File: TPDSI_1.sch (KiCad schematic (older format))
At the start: 2 parts, among them J1 Conn_01x02_Male, J2 Conn_01x02_Male

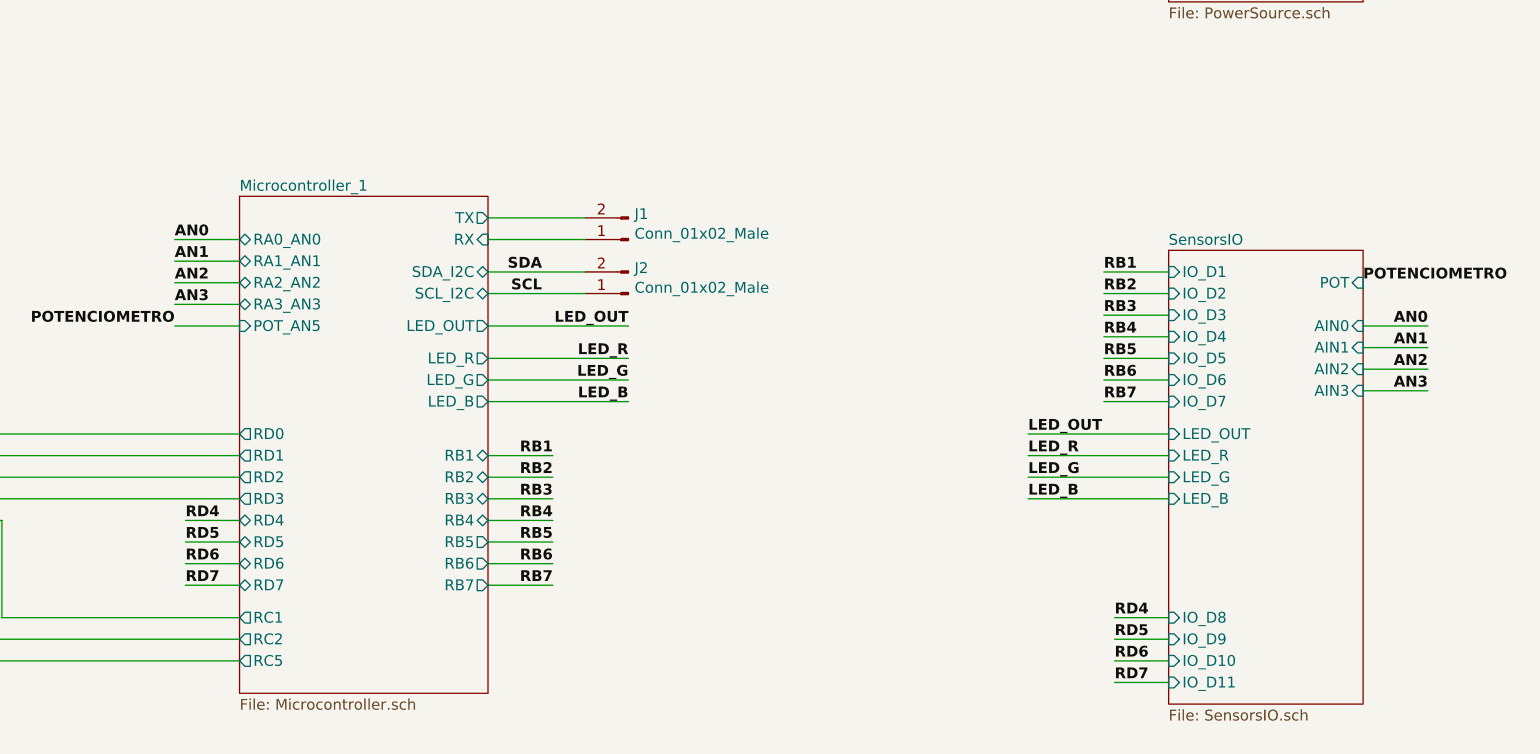
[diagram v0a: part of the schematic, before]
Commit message: Se agrega bus a jerarquia y pines de programación icsp
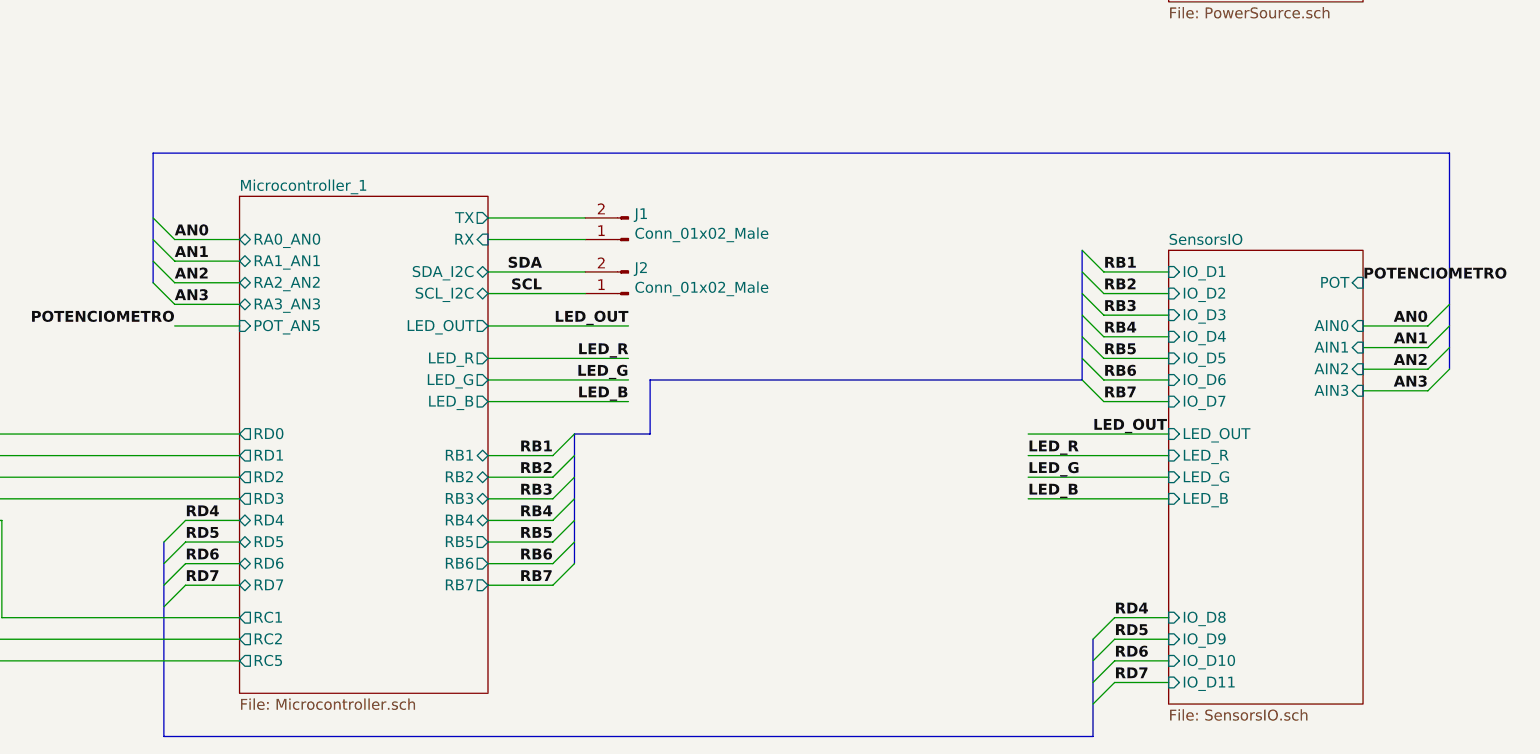
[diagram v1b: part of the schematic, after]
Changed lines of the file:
@@
 EESchema Schematic File Version 4
+LIBS:TPDSI_1-cache
 EELAYER 29 0
 EELAYER END
@@
 Sheet 1 5
 Title "Kit Development for MCU PIC"
-Date "2019-05-05"
-Rev "1.0"
+Date "2019-05-06"
+Rev "1.1"
 Comp "Julian Bustamante Narvaez"
 Comment1 ""
@@
 Wire Wire Line
 	4800 4800 5100 4800
-Text Label 5100 4200 2    50   ~ 10
-RB1
 Text Label 5100 4300 2    50   ~ 10
 RB2
@@
 POTENCIOMETRO
 Wire Wire Line
-	7950 4100 7300 4100
-Wire Wire Line
-	7950 4200 7300 4200
-Wire Wire Line
-	7950 4300 7300 4300
-Wire Wire Line
 	7950 4400 7300 4400
-Text Label 7300 4300 0    50   ~ 10
-LED_G
-Text Label 7300 4400 0    50   ~ 10
-LED_B
-Text Label 7300 4200 0    50   ~ 10
-LED_R
-Text Label 7300 4100 0    50   ~ 10
+Text Label 7600 4100 0    50   ~ 10
 LED_OUT
 Wire Wire Line
@@
 Text Label 7700 5250 0    50   ~ 10
 RD7
+Text Label 5100 4200 2    50   ~ 10
+RB1
+Entry Wire Line
+	5200 4100 5100 4200
+Entry Wire Line
+	5200 4200 5100 4300
+Entry Wire Line
+	5200 4300 5100 4400
+Entry Wire Line
+	5200 4400 5100 4500
+Entry Wire Line
+	5200 4500 5100 4600
+Entry Wire Line
+	5200 4600 5100 4700
+Entry Wire Line
+	5200 4700 5100 4800
+Entry Wire Line
+	3400 4500 3300 4600
+Entry Wire Line
+	3400 4600 3300 4700
+Entry Wire Line
+	3400 4700 3300 4800
+Entry Wire Line
+	3400 4800 3300 4900
+Entry Wire Line
+	7700 4950 7600 5050
+Entry Wire Line
+	7700 5050 7600 5150
+Entry Wire Line
+	7700 5150 7600 5250
+Entry Wire Line
+	7700 5250 7600 5350
+Wire Bus Line
+	3300 5500 7600 5500
+Entry Wire Line
+	3350 3500 3250 3400
+Entry Wire Line
+	3350 3400 3250 3300
+Entry Wire Line
+	3350 3300 3250 3200
+Entry Wire Line
+	3350 3200 3250 3100
+Entry Wire Line
+	9250 3500 9150 3600
+Entry Wire Line
+	9250 3600 9150 3700
+Entry Wire Line
+	9250 3700 9150 3800
+Entry Wire Line
+	9250 3800 9150 3900
+Wire Bus Line
+	9250 2800 3250 2800
+Entry Wire Line
+	7650 3350 7550 3250
+Entry Wire Line
+	7650 3450 7550 3350
+Entry Wire Line
+	7650 3550 7550 3450
+Entry Wire Line
+	7650 3650 7550 3550
+Entry Wire Line
+	7650 3750 7550 3650
+Entry Wire Line
+	7650 3850 7550 3750
+Entry Wire Line
+	7650 3950 7550 3850
+Text Label 7300 4200 0    50   ~ 10
+LED_R
+Text Label 7300 4400 0    50   ~ 10
+LED_B
+Text Label 7300 4300 0    50   ~ 10
+LED_G
+Wire Wire Line
+	7950 4300 7300 4300
+Wire Wire Line
+	7950 4200 7300 4200
+Wire Wire Line
+	7950 4100 7300 4100
+Wire Bus Line
+	7550 3850 5550 3850
+Wire Bus Line
+	5550 3850 5550 4100
+Wire Bus Line
+	5200 4100 5550 4100
+Wire Bus Line
+	9250 2800 9250 3800
+Wire Bus Line
+	3250 2800 3250 3400
+Wire Bus Line
+	7600 5050 7600 5500
+Wire Bus Line
+	3300 4600 3300 5500
+Wire Bus Line
+	5200 4100 5200 4700
+Wire Bus Line
+	7550 3250 7550 3850
 $EndSCHEMATC

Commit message: Se Organiza conexiones de alimentacion con elementos de la biblioteca power, se quitan algunas etiquetas y se coloca la fuente en hoja principal
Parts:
- added C1: 0.1uF, symbol Device:CP
- added C2: 22uF, symbol Device:CP
- added C3: 1uF, symbol Device:CP
- added C4: 10uF, symbol Device:CP
- added D1: D, symbol Device:D
- added D2: LED, symbol Device:LED
- added D3: D_TVS_DESD5V0S1BA-7DITR-ND, symbol Device:D_TVS
- added D6: D_TVS_3V3, symbol Device:D_TVS
- added J7: Conn_01x02_Male, symbol Connector:Conn_01x02_Male
- added R12: 330, symbol Device:R
- added U3: MC7805_TO252-3(DPACK), symbol J_ReguladorLinear:MC7805_TO252-3(DPACK)
- added U4: TLV2217_TO252-3, symbol J_ReguladorLinear:TLV2217_TO252-3
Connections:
- net labels added: +3.3V, +5V, 9V0, GND
- net labels removed: +3V3, +5V0
- wire segments 58 -> 90
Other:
- note added: "Power Source 5VDC and 3.3VDC"
- moved on the sheet: J1, J2

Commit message: Se agregan recomendaciones izq->dcha (In/Out), se Reorganiza jerarquía y bus de datos, se coloca graphics lines para indicar submodulos
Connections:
- wire segments 90 -> 80

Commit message: Se agrega ubicación de componentes, asociación de footprint, pendiente Ruteo.
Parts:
- C1: value 0.1uF -> 1uF; footprint (none) -> Capacitor_Tantalum_SMD:CP_EIA-3528-21_Kemet-B; Part Number (none) -> 399-14253-2-ND
- C2: footprint (none) -> Capacitor_Tantalum_SMD:CP_EIA-7343-20_Kemet-V; Part Number (none) -> P16517DKR-ND
- C3: footprint (none) -> Capacitor_Tantalum_SMD:CP_EIA-3528-21_Kemet-B
- C4: footprint (none) -> Capacitor_Tantalum_SMD:CP_EIA-7343-20_Kemet-V; Part number (none) -> 399-16038-1-ND
- D1: footprint (none) -> Diode_SMD:D_SOD-123; PArt Number (none) -> 1N4148W-FDICT-ND
- D2: footprint (none) -> LED_SMD:LED_0603_1608Metric_Castellated; PArt Number (none) -> 160-1446-6-ND
- D3: footprint (none) -> Diode_SMD:D_SOD-123
- D6: footprint (none) -> Diode_SMD:D_SOD-123; Part Number (none) -> 641-1985-1-ND
- J1, J2, J7: footprint (none) -> Connector_PinSocket_2.54mm:PinSocket_1x02_P2.54mm_Vertical
- R12: footprint (none) -> Resistor_SMD:R_0603_1608Metric_Pad1.05x0.95mm_HandSolder
- U3, U4: footprint (none) -> Package_TO_SOT_SMD:TO-252-2
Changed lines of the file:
@@
 AR Path="/5CDBB83D" Ref="C1"  Part="1"
 F 0 "C1" H 2168 1596 50  0000 L CNN
-F 1 "0.1uF" H 2168 1505 50  0000 L CNN
-F 2 "" H 2088 1400 50  0001 C CNN
+F 1 "1uF" H 2168 1505 50  0000 L CNN
+F 2 "Capacitor_Tantalum_SMD:CP_EIA-3528-21_Kemet-B" H 2088 1400 50  0001 C CNN
 F 3 "~" H 2050 1550 50  0001 C CNN
+F 4 "	399-14253-2-ND" H 2050 1550 50  0001 C CNN "Part Number"
 	1    2050 1550
 	1    0    0    -1
@@
 F 0 "C2" H 3018 1596 50  0000 L CNN
 F 1 "22uF" H 3018 1505 50  0000 L CNN
-F 2 "" H 2938 1400 50  0001 C CNN
+F 2 "Capacitor_Tantalum_SMD:CP_EIA-7343-20_Kemet-V" H 2938 1400 50  0001 C CNN
 F 3 "~" H 2900 1550 50  0001 C CNN
+F 4 "P16517DKR-ND" H 2900 1550 50  0001 C CNN "Part Number"
 	1    2900 1550
 	1    0    0    -1
@@
 F 0 "U4" H 4200 1215 50  0000 C CNN
 F 1 "TLV2217_TO252-3" H 4200 1124 50  0000 C CNN
-F 2 "" H 4000 1050 50  0001 C CNN
+F 2 "Package_TO_SOT_SMD:TO-252-2" H 4000 1050 50  0001 C CNN
 F 3 "http://www.ti.com/lit/ds/symlink/tlv2217.pdf" H 4000 1050 50  0001 C CNN
 F 4 "296-19786-1-ND" H 4000 1100 50  0001 C CNN " Part Number"
@@
 AR Path="/5CCF7078/5CDBB851" Ref="U?"  Part="1"
 AR Path="/5CDBB851" Ref="U3"  Part="1"
+AR Path="/5CCF70C1/5CDBB851" Ref="U3"  Part="1"
 F 0 "U3" H 2450 1215 50  0000 C CNN
 F 1 "MC7805_TO252-3(DPACK)" H 2450 1124 50  0000 C CNN
-F 2 "" H 2250 1050 50  0001 C CNN
+F 2 "Package_TO_SOT_SMD:TO-252-2" H 2250 1050 50  0001 C CNN
 F 3 "https://www.onsemi.com/pub/Collateral/MC7800-D.PDF" H 2250 1050 50  0001 C CNN
 F 4 "MC7805BDTRKGOSCT-ND" H 2450 1300 50  0001 C CNN " Part Number"
@@
 F 0 "C3" H 3818 1596 50  0000 L CNN
 F 1 "1uF" H 3818 1505 50  0000 L CNN
-F 2 "" H 3738 1400 50  0001 C CNN
+F 2 "Capacitor_Tantalum_SMD:CP_EIA-3528-21_Kemet-B" H 3738 1400 50  0001 C CNN
 F 3 "~" H 3700 1550 50  0001 C CNN
 	1    3700 1550
@@
 F 0 "C4" H 4768 1596 50  0000 L CNN
 F 1 "10uF" H 4768 1505 50  0000 L CNN
-F 2 "" H 4688 1400 50  0001 C CNN
+F 2 "Capacitor_Tantalum_SMD:CP_EIA-7343-20_Kemet-V" H 4688 1400 50  0001 C CNN
 F 3 "~" H 4650 1550 50  0001 C CNN
+F 4 "399-16038-1-ND" H 4650 1550 50  0001 C CNN "Part number"
 	1    4650 1550
 	1    0    0    -1
@@
 F 0 "D1" H 1550 1366 50  0000 C CNN
 F 1 "D" H 1550 1275 50  0000 C CNN
-F 2 "" H 1550 1150 50  0001 C CNN
+F 2 "Diode_SMD:D_SOD-123" H 1550 1150 50  0001 C CNN
 F 3 "~" H 1550 1150 50  0001 C CNN
+F 4 "1N4148W-FDICT-ND" H 1550 1150 50  0001 C CNN "PArt Number"
 	1    1550 1150
 	-1   0    0    -1
@@
 F 0 "D6" V 5104 1629 50  0000 L CNN
 F 1 "D_TVS_3V3" H 5000 1850 50  0000 L CNN
-F 2 "" H 5150 1550 50  0001 C CNN
+F 2 "Diode_SMD:D_SOD-123" H 5150 1550 50  0001 C CNN
 F 3 "~" H 5150 1550 50  0001 C CNN
+F 4 "641-1985-1-ND" V 5150 1550 50  0001 C CNN "Part Number"
 	1    5150 1550
 	0    1    1    0
@@
 F 0 "D2" V 1789 1583 50  0000 R CNN
 F 1 "LED" V 1698 1583 50  0000 R CNN
-F 2 "" H 1750 1700 50  0001 C CNN
+F 2 "LED_SMD:LED_0603_1608Metric_Castellated" H 1750 1700 50  0001 C CNN
 F 3 "~" H 1750 1700 50  0001 C CNN
+F 4 "	160-1446-6-ND" V 1750 1700 50  0001 C CNN "PArt Number"
 	1    1750 1700
 	0    -1   -1   0
@@
 F 0 "R12" H 1820 1346 50  0000 L CNN
 F 1 "330" H 1820 1255 50  0000 L CNN
-F 2 "" V 1680 1300 50  0001 C CNN
+F 2 "Resistor_SMD:R_0603_1608Metric_Pad1.05x0.95mm_HandSolder" V 1680 1300 50  0001 C CNN
 F 3 "~" H 1750 1300 50  0001 C CNN
 	1    1750 1300
@@
 F 0 "D3" V 3154 1629 50  0000 L CNN
 F 1 "D_TVS_DESD5V0S1BA-7DITR-ND" V 3800 750 50  0001 L CNN
-F 2 "" H 3200 1550 50  0001 C CNN
+F 2 "Diode_SMD:D_SOD-123" H 3200 1550 50  0001 C CNN
 F 3 "~" H 3200 1550 50  0001 C CNN
 	1    3200 1550
@@
 F 0 "J7" H 1150 1350 50  0000 C CNN
 F 1 "Conn_01x02_Male" H 1000 950 50  0000 C CNN
-F 2 "" H 1050 1150 50  0001 C CNN
+F 2 "Connector_PinSocket_2.54mm:PinSocket_1x02_P2.54mm_Vertical" H 1050 1150 50  0001 C CNN
 F 3 "~" H 1050 1150 50  0001 C CNN
 	1    1050 1150
@@
 F 0 "J1" H 7322 3732 50  0000 R CNN
 F 1 "Conn_01x02_Male" H 7322 3823 50  0000 R CNN
-F 2 "" H 7350 3850 50  0001 C CNN
+F 2 "Connector_PinSocket_2.54mm:PinSocket_1x02_P2.54mm_Vertical" H 7350 3850 50  0001 C CNN
 F 3 "~" H 7350 3850 50  0001 C CNN
 	1    7350 3850
@@
 F 0 "J2" H 7322 3982 50  0000 R CNN
 F 1 "Conn_01x02_Male" H 7322 4073 50  0000 R CNN
-F 2 "" H 7350 4100 50  0001 C CNN
+F 2 "Connector_PinSocket_2.54mm:PinSocket_1x02_P2.54mm_Vertical" H 7350 4100 50  0001 C CNN
 F 3 "~" H 7350 4100 50  0001 C CNN
 	1    7350 4100

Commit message: Se reorganiza componenentes lineas mas limpias y analógicas mas cerca,Se cambia potenciometro y bornera de alimentación, se colocan perforaciones en la tarjeta
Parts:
- removed J7: Conn_01x02_Male, Connector_PinSocket_2.54mm:PinSocket_1x02_P2.54mm_Vertical, symbol Connector:Conn_01x02_Male
- added H1, H2, H3, H4: MountingHole, MountingHole:MountingHole_3.2mm_M3, symbol Mechanical:MountingHole
- added J7: Screw_Terminal_01x02, TerminalBlock:TerminalBlock_bornier-2_P5.08mm, symbol Connector:Screw_Terminal_01x02
- U3: symbol J_ReguladorLinear:MC7805_TO252-3(DPACK) -> TPDSI_1-rescue:MC7805_TO252-3(DPACK)-J_ReguladorLinear
- U4: symbol J_ReguladorLinear:TLV2217_TO252-3 -> TPDSI_1-rescue:TLV2217_TO252-3-J_ReguladorLinear
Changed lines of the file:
@@
 $EndComp
 $Comp
-L J_ReguladorLinear:TLV2217_TO252-3 U?
+L TPDSI_1-rescue:TLV2217_TO252-3-J_ReguladorLinear U?
 U 1 1 5CDBB84A
 P 4000 1050
@@
 $EndComp
 $Comp
-L J_ReguladorLinear:MC7805_TO252-3(DPACK) U?
+L TPDSI_1-rescue:MC7805_TO252-3(DPACK)-J_ReguladorLinear U?
 U 1 1 5CDBB851
 P 2250 1050
@@
 Wire Wire Line
 	1350 1250 1350 1800
-$Comp
-L Connector:Conn_01x02_Male J7
-U 1 1 5CF0DD35
-P 1050 1150
-F 0 "J7" H 1150 1350 50  0000 C CNN
-F 1 "Conn_01x02_Male" H 1000 950 50  0000 C CNN
-F 2 "Connector_PinSocket_2.54mm:PinSocket_1x02_P2.54mm_Vertical" H 1050 1150 50  0001 C CNN
-F 3 "~" H 1050 1150 50  0001 C CNN
-	1    1050 1150
-	1    0    0    -1
-$EndComp
 Text Label 1300 1150 0    50   ~ 0
 9V0
@@
 Wire Wire Line
 	3650 5850 5550 5850
+$Comp
+L Connector:Screw_Terminal_01x02 J7
+U 1 1 5CF6B993
+P 1050 1250
+F 0 "J7" H 968 925 50  0000 C CNN
+F 1 "Screw_Terminal_01x02" H 968 1016 50  0000 C CNN
+F 2 "TerminalBlock:TerminalBlock_bornier-2_P5.08mm" H 1050 1250 50  0001 C CNN
+F 3 "~" H 1050 1250 50  0001 C CNN
+	1    1050 1250
+	-1   0    0    1
+$EndComp
+$Comp
+L Mechanical:MountingHole H1
+U 1 1 5CF85774
+P 10050 1000
+F 0 "H1" H 10150 1046 50  0000 L CNN
+F 1 "MountingHole" H 10150 955 50  0000 L CNN
+F 2 "MountingHole:MountingHole_3.2mm_M3" H 10050 1000 50  0001 C CNN
+F 3 "~" H 10050 1000 50  0001 C CNN
+	1    10050 1000
+	1    0    0    -1
+$EndComp
+$Comp
+L Mechanical:MountingHole H2
+U 1 1 5CF8F6CA
+P 10050 1300
+F 0 "H2" H 10150 1346 50  0000 L CNN
+F 1 "MountingHole" H 10150 1255 50  0000 L CNN
+F 2 "MountingHole:MountingHole_3.2mm_M3" H 10050 1300 50  0001 C CNN
+F 3 "~" H 10050 1300 50  0001 C CNN
+	1    10050 1300
+	1    0    0    -1
+$EndComp
+$Comp
+L Mechanical:MountingHole H3
+U 1 1 5CF918E9
+P 10050 1600
+F 0 "H3" H 10150 1646 50  0000 L CNN
+F 1 "MountingHole" H 10150 1555 50  0000 L CNN
+F 2 "MountingHole:MountingHole_3.2mm_M3" H 10050 1600 50  0001 C CNN
+F 3 "~" H 10050 1600 50  0001 C CNN
+	1    10050 1600
+	1    0    0    -1
+$EndComp
+$Comp
+L Mechanical:MountingHole H4
+U 1 1 5CF93C5D
+P 10050 1850
+F 0 "H4" H 10150 1896 50  0000 L CNN
+F 1 "MountingHole" H 10150 1805 50  0000 L CNN
+F 2 "MountingHole:MountingHole_3.2mm_M3" H 10050 1850 50  0001 C CNN
+F 3 "~" H 10050 1850 50  0001 C CNN
+	1    10050 1850
+	1    0    0    -1
+$EndComp
 Wire Bus Line
 	4050 3750 4050 4050

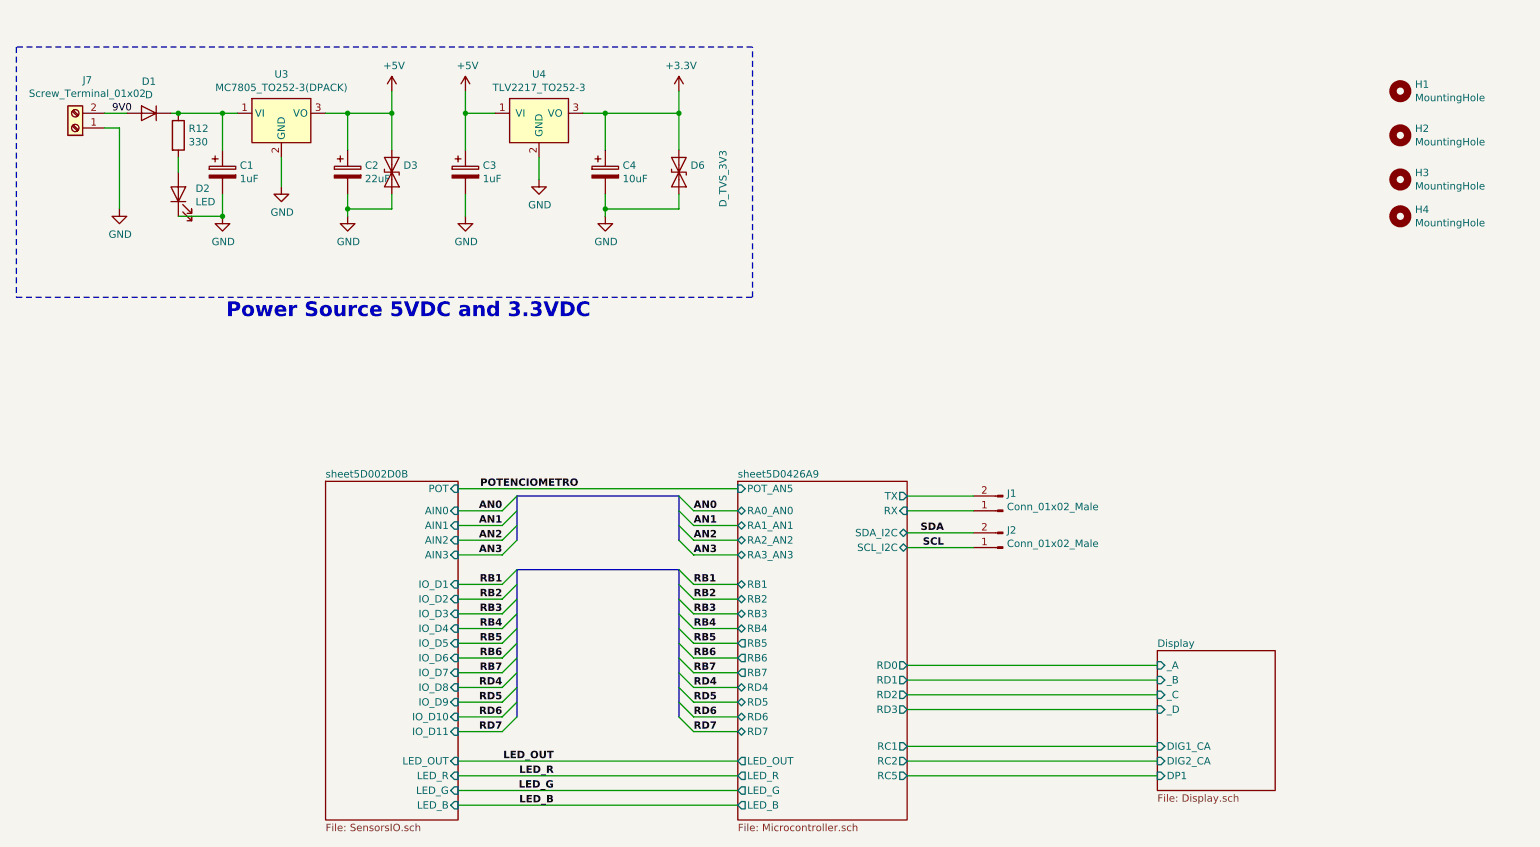
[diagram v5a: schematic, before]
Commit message: Se agrega recomendaciones  de jacobo salvador
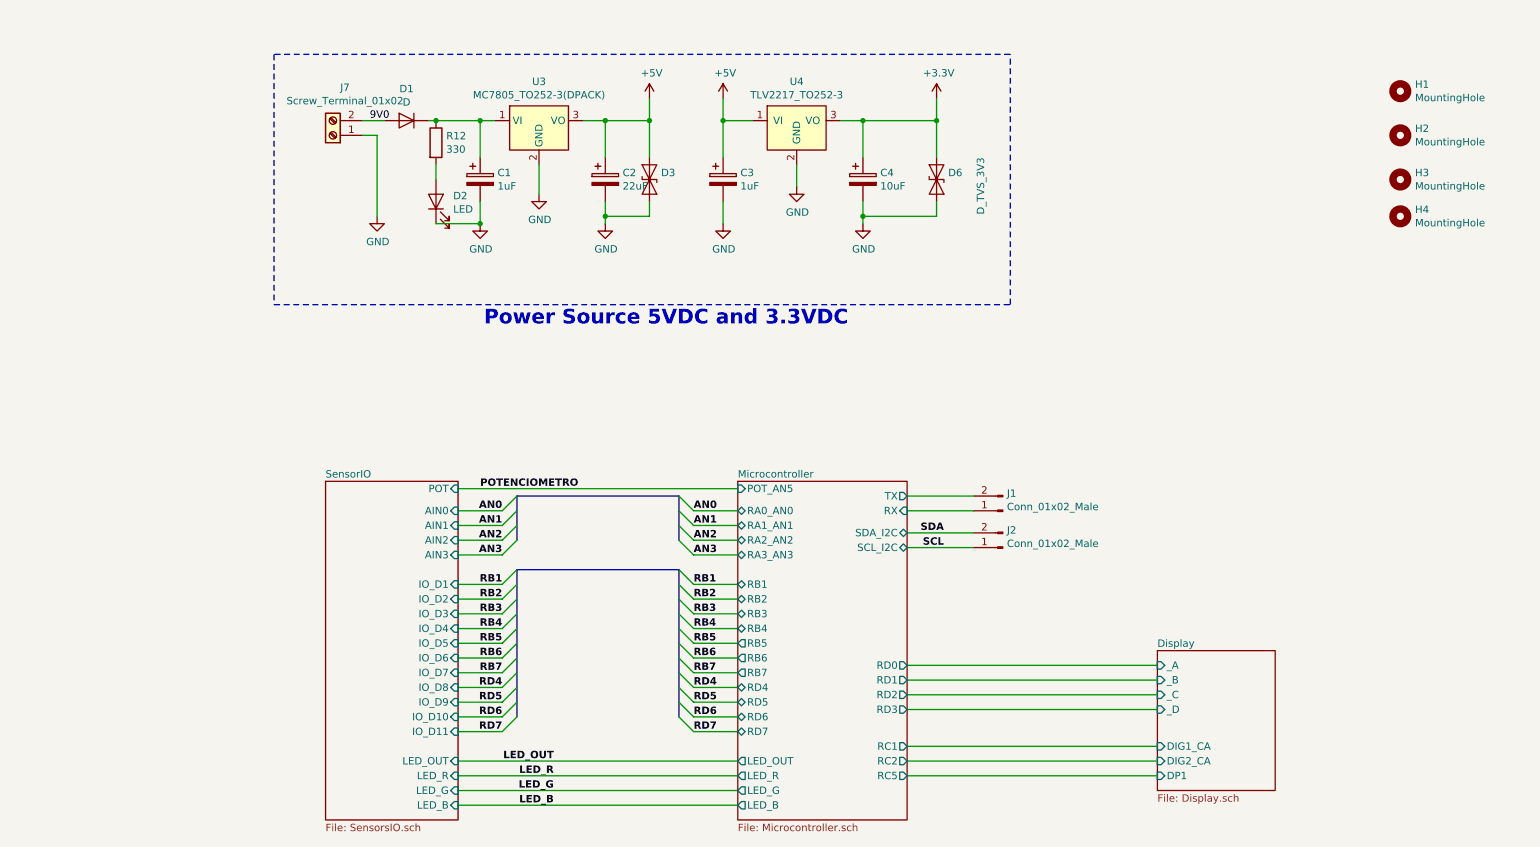
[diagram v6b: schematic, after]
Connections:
- net sheet5D0426A9/RX renamed Microcontroller/RX
- net sheet5D0426A9/TX renamed Microcontroller/TX
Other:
- moved on the sheet: C1, C2, C3, C4, D1, D2, D3, D6, J7, R12, U3, U4
